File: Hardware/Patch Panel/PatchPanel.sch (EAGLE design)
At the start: 49 parts

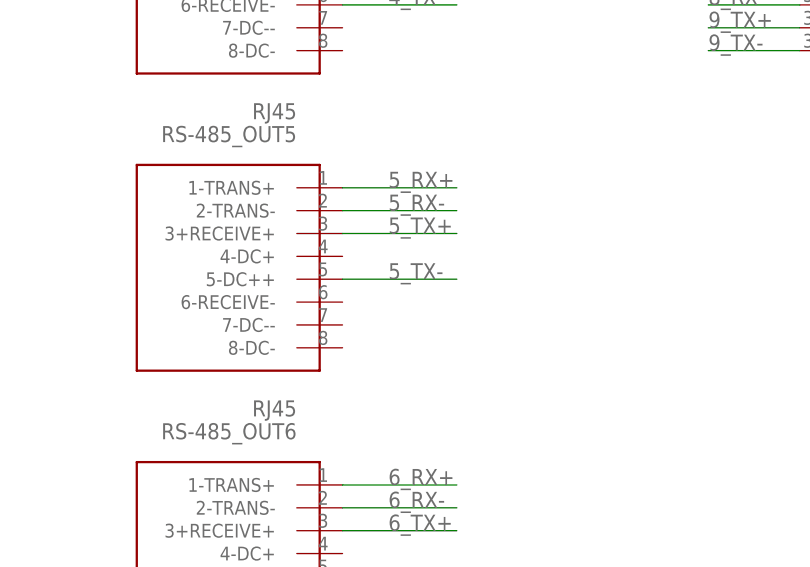
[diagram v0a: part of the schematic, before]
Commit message: Issue #49 Patch Panel RJ-45 port number 5 Fixed the incorrect wires on board file and schematic file.
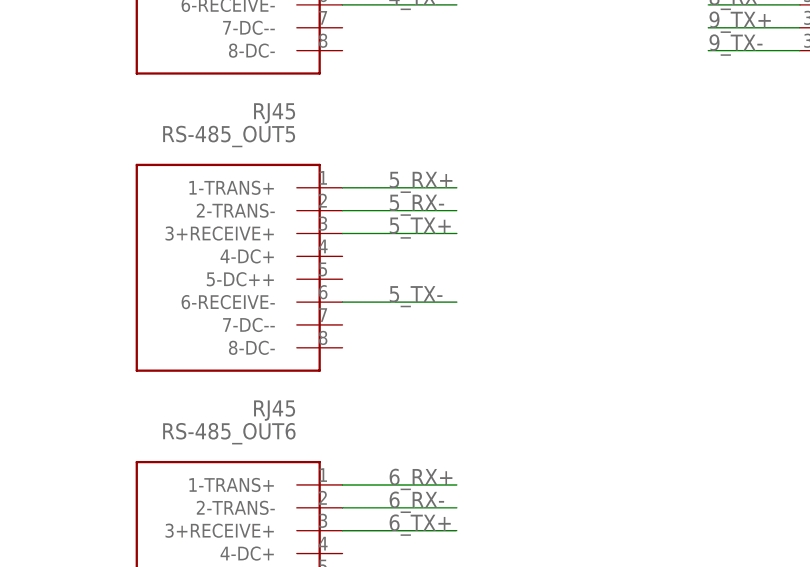
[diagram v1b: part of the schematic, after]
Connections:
- net 5_TX-: now also RS-485_OUT5.6-RECEIVE-; no longer RS-485_OUT5.5-DC++
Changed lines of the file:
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@@
 <?xml version="1.0" encoding="utf-8"?>
 <!DOCTYPE eagle SYSTEM "eagle.dtd">
-<eagle version="6.2">
+<eagle version="6.5.0">
 <drawing>
 <settings>
@@
 </segment>
 <segment>
-<pinref part="RS-485_OUT5" gate="G$1" pin="5-DC++"/>
-<wire x1="71.12" y1="15.24" x2="83.82" y2="15.24" width="0.1524" layer="91"/>
-<label x="76.2" y="15.24" size="1.778" layer="95"/>
-</segment>
-</net>
+<pinref part="RS-485_OUT5" gate="G$1" pin="6-RECEIVE-"/>
+<wire x1="71.12" y1="12.7" x2="83.82" y2="12.7" width="0.1524" layer="91"/>
+<label x="76.2" y="12.7" size="1.778" layer="95"/>
+</segment>
+</net>
